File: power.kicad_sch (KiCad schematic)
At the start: 75 parts, among them SW1 SW_Push, U3 BD71847MWV, U4 NCP718BSN250T1G, Y1 Crystal

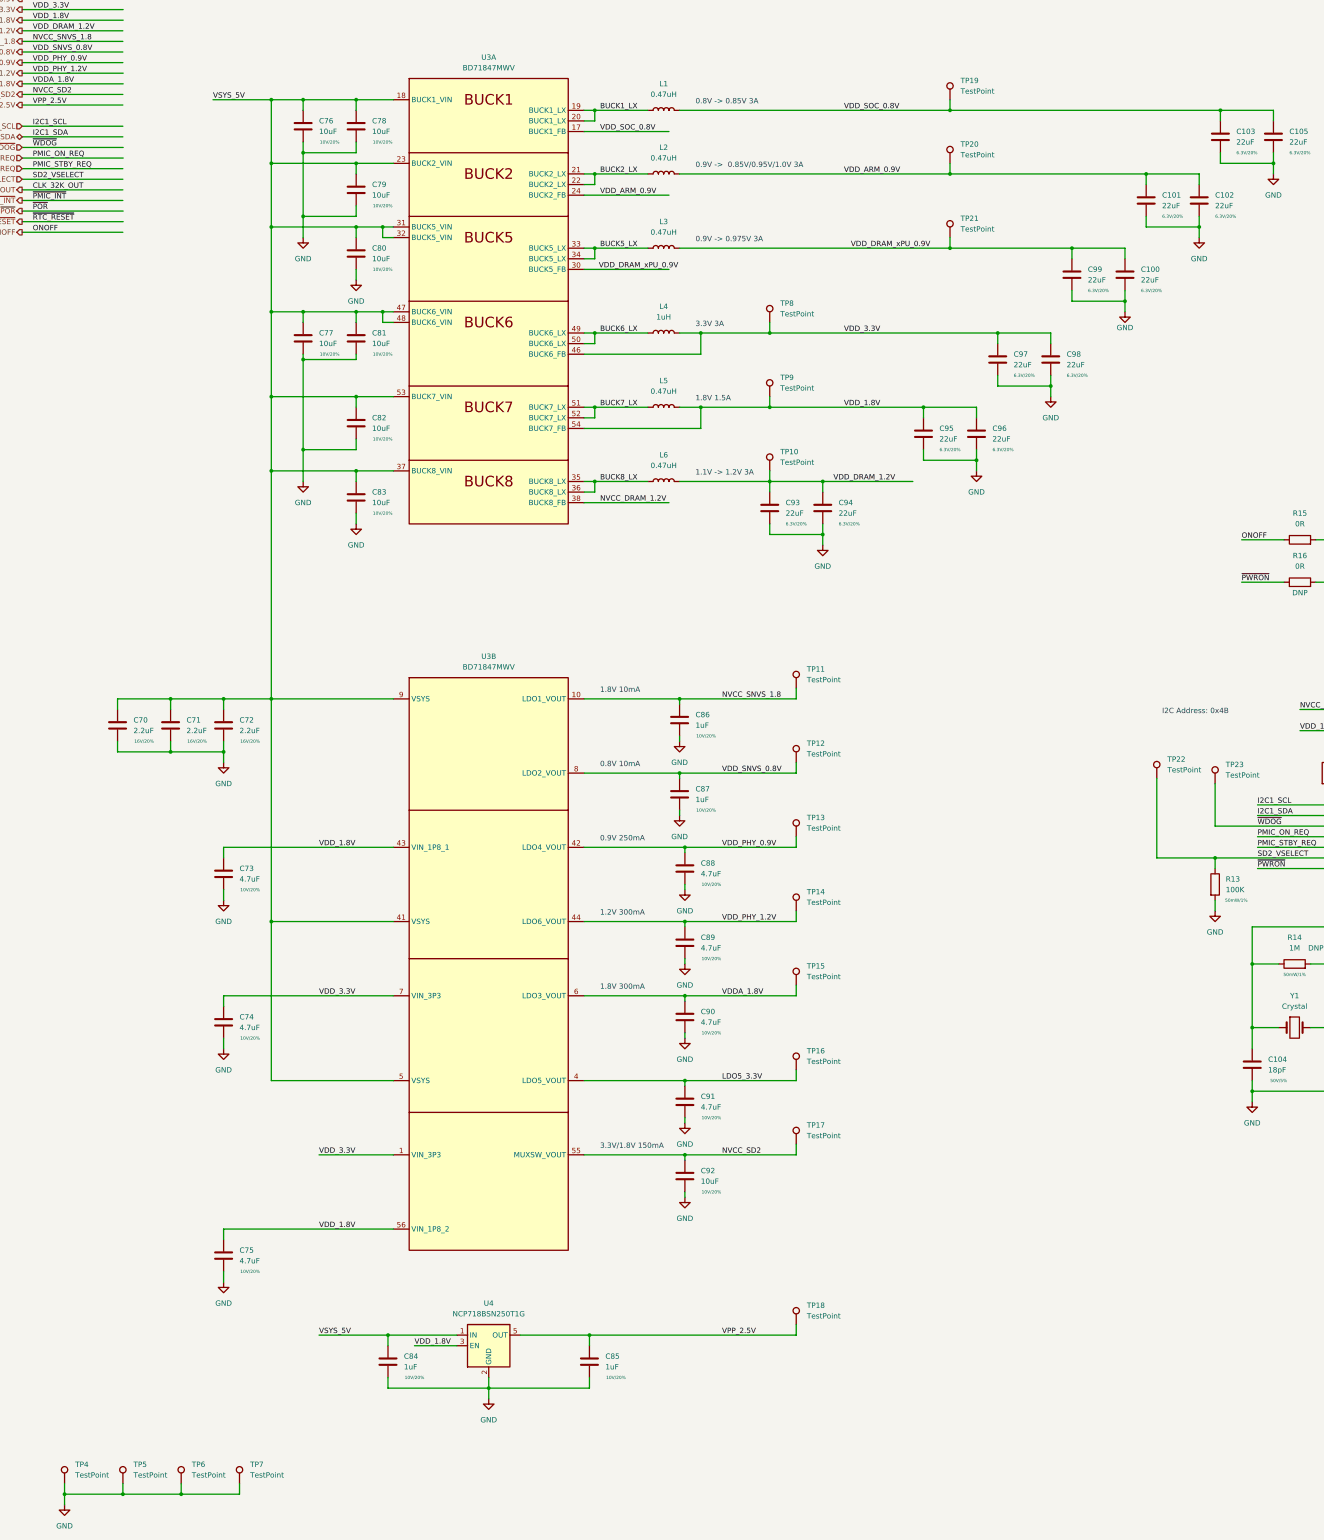
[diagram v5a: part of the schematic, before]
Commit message: v2 of ddr flytimes tool, lots of routing work, sch fixes
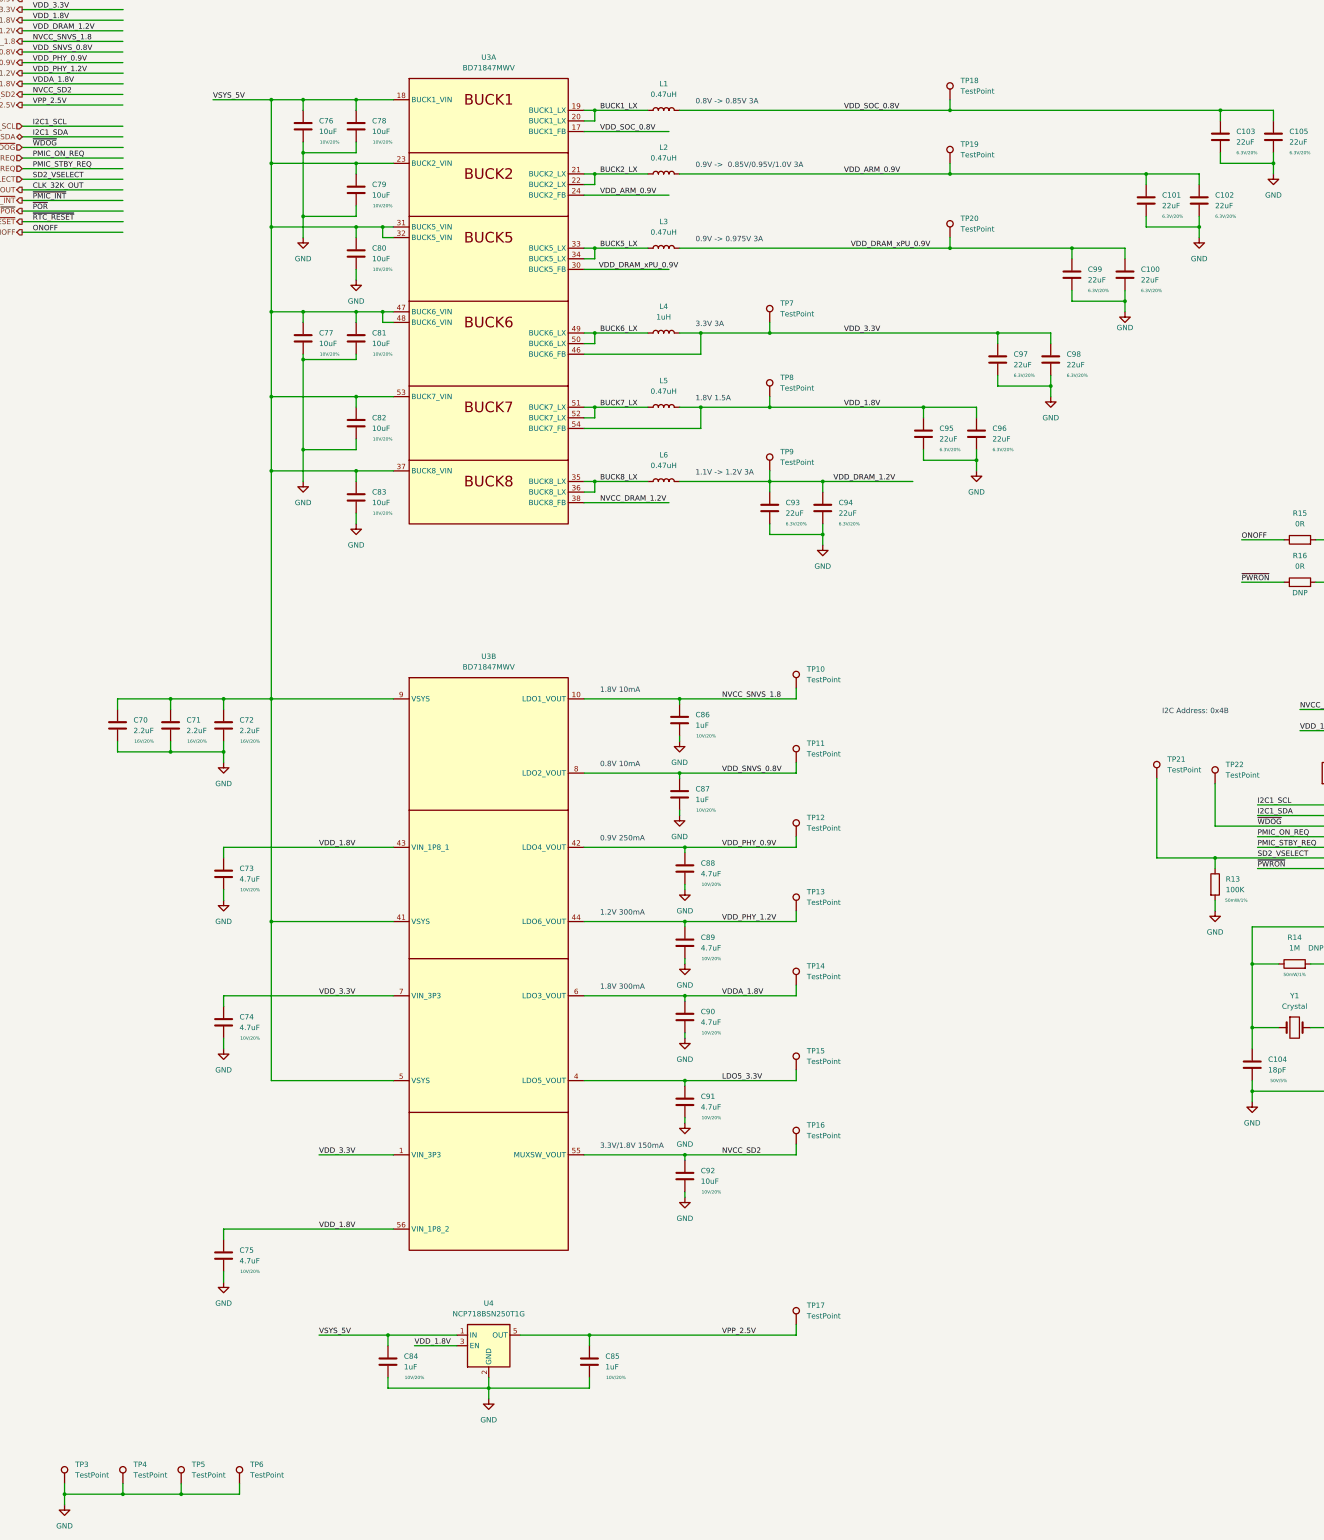
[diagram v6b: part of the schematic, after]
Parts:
- renumbered TP11 to TP10, TP12 to TP11, TP13 to TP12, TP14 to TP13, TP15 to TP14, TP16 to TP15, TP17 to TP16, TP18 to TP17, TP19 to TP18, TP20 to TP19, TP21 to TP20, TP22 to TP21, TP23 to TP22, TP4 to TP3, TP5 to TP4, TP6 to TP5, TP7 to TP6, TP8 to TP7, TP9 to TP8, TP10 to TP9
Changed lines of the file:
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@@
   (symbol (lib_id "Connector:TestPoint") (at 257.81 49.53 0) (unit 1)
     (in_bom yes) (on_board yes) (fields_autoplaced)
-    (property "Reference" "TP19" (id 0) (at 260.35 44.9579 0)
+    (property "Reference" "TP18" (id 0) (at 260.35 44.9579 0)
       (effects (font (size 1.27 1.27)) (justify left))
     )
@@
   (symbol (lib_id "Connector:TestPoint") (at 73.66 381 0) (unit 1)
     (in_bom yes) (on_board yes) (fields_autoplaced)
-    (property "Reference" "TP6" (id 0) (at 76.2 376.4279 0)
+    (property "Reference" "TP5" (id 0) (at 76.2 376.4279 0)
       (effects (font (size 1.27 1.27)) (justify left))
     )
@@
   (symbol (lib_id "Connector:TestPoint") (at 220.98 281.94 0) (unit 1)
     (in_bom yes) (on_board yes) (fields_autoplaced)
-    (property "Reference" "TP16" (id 0) (at 223.52 277.3679 0)
+    (property "Reference" "TP15" (id 0) (at 223.52 277.3679 0)
       (effects (font (size 1.27 1.27)) (justify left))
     )
@@
   (symbol (lib_id "Connector:TestPoint") (at 220.98 226.06 0) (unit 1)
     (in_bom yes) (on_board yes) (fields_autoplaced)
-    (property "Reference" "TP13" (id 0) (at 223.52 221.4879 0)
+    (property "Reference" "TP12" (id 0) (at 223.52 221.4879 0)
       (effects (font (size 1.27 1.27)) (justify left))
     )
@@
   (symbol (lib_id "Connector:TestPoint") (at 59.69 381 0) (unit 1)
     (in_bom yes) (on_board yes) (fields_autoplaced)
-    (property "Reference" "TP5" (id 0) (at 62.23 376.4279 0)
+    (property "Reference" "TP4" (id 0) (at 62.23 376.4279 0)
       (effects (font (size 1.27 1.27)) (justify left))
     )
@@
   (symbol (lib_id "Connector:TestPoint") (at 45.72 381 0) (unit 1)
     (in_bom yes) (on_board yes) (fields_autoplaced)
-    (property "Reference" "TP4" (id 0) (at 48.26 376.4279 0)
+    (property "Reference" "TP3" (id 0) (at 48.26 376.4279 0)
       (effects (font (size 1.27 1.27)) (justify left))
     )
@@
   (symbol (lib_id "Connector:TestPoint") (at 220.98 299.72 0) (unit 1)
     (in_bom yes) (on_board yes) (fields_autoplaced)
-    (property "Reference" "TP17" (id 0) (at 223.52 295.1479 0)
+    (property "Reference" "TP16" (id 0) (at 223.52 295.1479 0)
       (effects (font (size 1.27 1.27)) (justify left))
     )
@@
   (symbol (lib_id "Connector:TestPoint") (at 214.63 102.87 0) (unit 1)
     (in_bom yes) (on_board yes) (fields_autoplaced)
-    (property "Reference" "TP8" (id 0) (at 217.17 98.2979 0)
+    (property "Reference" "TP7" (id 0) (at 217.17 98.2979 0)
       (effects (font (size 1.27 1.27)) (justify left))
     )
@@
   (symbol (lib_id "Connector:TestPoint") (at 220.98 342.9 0) (unit 1)
     (in_bom yes) (on_board yes) (fields_autoplaced)
-    (property "Reference" "TP18" (id 0) (at 223.52 338.3279 0)
+    (property "Reference" "TP17" (id 0) (at 223.52 338.3279 0)
       (effects (font (size 1.27 1.27)) (justify left))
     )
@@
   (symbol (lib_id "Connector:TestPoint") (at 257.81 82.55 0) (unit 1)
     (in_bom yes) (on_board yes) (fields_autoplaced)
-    (property "Reference" "TP21" (id 0) (at 260.35 77.9779 0)
+    (property "Reference" "TP20" (id 0) (at 260.35 77.9779 0)
       (effects (font (size 1.27 1.27)) (justify left))
     )
@@
   (symbol (lib_id "Connector:TestPoint") (at 220.98 261.62 0) (unit 1)
     (in_bom yes) (on_board yes) (fields_autoplaced)
-    (property "Reference" "TP15" (id 0) (at 223.52 257.0479 0)
+    (property "Reference" "TP14" (id 0) (at 223.52 257.0479 0)
       (effects (font (size 1.27 1.27)) (justify left))
     )
@@
   (symbol (lib_id "Connector:TestPoint") (at 220.98 190.5 0) (unit 1)
     (in_bom yes) (on_board yes) (fields_autoplaced)
-    (property "Reference" "TP11" (id 0) (at 223.52 185.9279 0)
+    (property "Reference" "TP10" (id 0) (at 223.52 185.9279 0)
       (effects (font (size 1.27 1.27)) (justify left))
     )
@@
   (symbol (lib_id "Connector:TestPoint") (at 214.63 120.65 0) (unit 1)
     (in_bom yes) (on_board yes) (fields_autoplaced)
-    (property "Reference" "TP9" (id 0) (at 217.17 116.0779 0)
+    (property "Reference" "TP8" (id 0) (at 217.17 116.0779 0)
       (effects (font (size 1.27 1.27)) (justify left))
     )
@@
   (symbol (lib_id "Connector:TestPoint") (at 257.81 64.77 0) (unit 1)
     (in_bom yes) (on_board yes) (fields_autoplaced)
-    (property "Reference" "TP20" (id 0) (at 260.35 60.1979 0)
+    (property "Reference" "TP19" (id 0) (at 260.35 60.1979 0)
       (effects (font (size 1.27 1.27)) (justify left))
     )
@@
   (symbol (lib_id "Connector:TestPoint") (at 220.98 208.28 0) (unit 1)
     (in_bom yes) (on_board yes) (fields_autoplaced)
-    (property "Reference" "TP12" (id 0) (at 223.52 203.7079 0)
+    (property "Reference" "TP11" (id 0) (at 223.52 203.7079 0)
       (effects (font (size 1.27 1.27)) (justify left))
     )
@@
   (symbol (lib_id "Connector:TestPoint") (at 87.63 381 0) (unit 1)
     (in_bom yes) (on_board yes) (fields_autoplaced)
-    (property "Reference" "TP7" (id 0) (at 90.17 376.4279 0)
+    (property "Reference" "TP6" (id 0) (at 90.17 376.4279 0)
       (effects (font (size 1.27 1.27)) (justify left))
     )
@@
   (symbol (lib_id "Connector:TestPoint") (at 220.98 243.84 0) (unit 1)
     (in_bom yes) (on_board yes) (fields_autoplaced)
-    (property "Reference" "TP14" (id 0) (at 223.52 239.2679 0)
+    (property "Reference" "TP13" (id 0) (at 223.52 239.2679 0)
       (effects (font (size 1.27 1.27)) (justify left))
     )
@@
   (symbol (lib_id "Connector:TestPoint") (at 307.34 212.09 0) (unit 1)
     (in_bom yes) (on_board yes) (fields_autoplaced)
-    (property "Reference" "TP22" (id 0) (at 309.88 207.5179 0)
+    (property "Reference" "TP21" (id 0) (at 309.88 207.5179 0)
       (effects (font (size 1.27 1.27)) (justify left))
     )
@@
   (symbol (lib_id "Connector:TestPoint") (at 321.31 213.36 0) (unit 1)
     (in_bom yes) (on_board yes) (fields_autoplaced)
-    (property "Reference" "TP23" (id 0) (at 323.85 208.7879 0)
+    (property "Reference" "TP22" (id 0) (at 323.85 208.7879 0)
       (effects (font (size 1.27 1.27)) (justify left))
     )
@@
   (symbol (lib_id "Connector:TestPoint") (at 214.63 138.43 0) (unit 1)
     (in_bom yes) (on_board yes) (fields_autoplaced)
-    (property "Reference" "TP10" (id 0) (at 217.17 133.8579 0)
-      (effects (font (size 1.27 1.27)) (justify left))
-    )
+    (property "Reference" "TP9" (id 0) (at 217.17 133.8579 0)
+      (effects (font (size 1.27 1.27)) (justify left))
+    )

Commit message: inital routing of ddr data bus, sch work
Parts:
- removed C84, C85: 1uF, Capacitor_SMD:C_0402_1005Metric, symbol Device:C
- removed TP17: TestPoint, TestPoint:TestPoint_Pad_D1.0mm, symbol Connector:TestPoint
- removed U4: NCP718BSN250T1G, Package_TO_SOT_SMD:SOT-23-5, symbol Regulator_Linear:NCP718xSN250
- renumbered C70 to C58, C71 to C59, C72 to C60, C73 to C61, C74 to C62, C75 to C63, C76 to C64, C77 to C65, C78 to C66, C79 to C67, C80 to C68, C81 to C69, C82 to C70, C83 to C71, C86 to C72, C87 to C73, C88 to C74, C89 to C75, C90 to C76, C91 to C77, C92 to C78, C93 to C79, C94 to C80, C95 to C81, C96 to C82, C97 to C83, C98 to C84, C99 to C85, C100 to C86, C101 to C87, C102 to C88, C103 to C89, C104 to C90, C105 to C91, C106 to C92, C107 to C93, C108 to C94, R13 to R11, R14 to R12, R15 to R13, R16 to R14, R17 to R15, R18 to R16, TP11 to TP10, TP12 to TP11, TP13 to TP12, TP14 to TP13, TP15 to TP14, TP16 to TP15, TP18 to TP16, TP19 to TP17, TP20 to TP18, TP21 to TP19, TP3 to TP2, TP22 to TP20, TP4 to TP3, TP5 to TP4, TP6 to TP5, TP7 to TP6, TP8 to TP7, TP9 to TP8, TP10 to TP9
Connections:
- net VDD_DRAM_1.2V renamed VDD_DRAM_1.1V

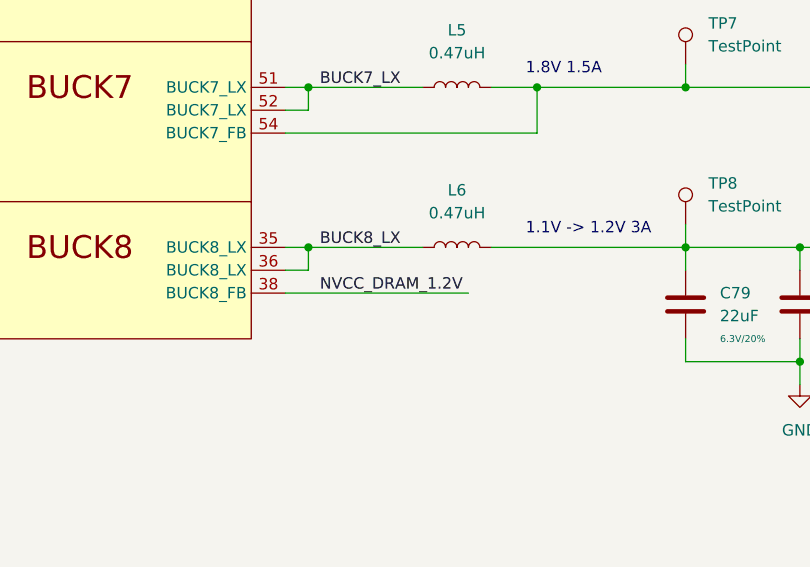
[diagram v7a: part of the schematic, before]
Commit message: add SN65DSI86 DSI2DP ic, SCH, PCB work, flytime work
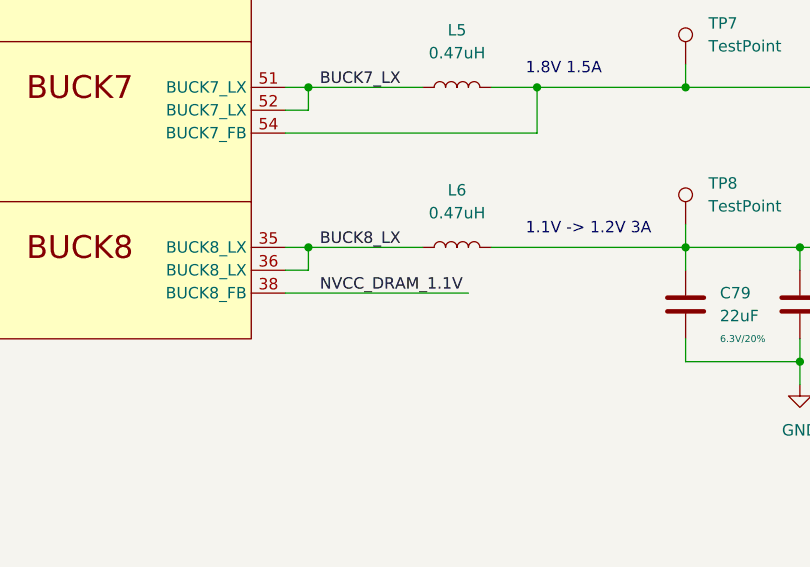
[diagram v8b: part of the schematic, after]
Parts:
- SW1: footprint Button_Switch_THT:SW_Tactile_SPST_Angled_PTS645Vx58-2LFS -> Button_Switch_SMD:SW_SPST_EVQP7A
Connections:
- net NVCC_DRAM_1.2V renamed NVCC_DRAM_1.1V
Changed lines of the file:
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@@
     (effects (font (size 1.27 1.27)) (justify left bottom))
   )
-  (label "NVCC_DRAM_1.2V" (at 173.99 146.05 0)
+  (label "NVCC_DRAM_1.1V" (at 173.99 146.05 0)
     (effects (font (size 1.27 1.27)) (justify left bottom))
   )
@@
     (property "Reference" "SW1" (id 0) (at 360.68 147.32 0))
     (property "Value" "SW_Push" (id 1) (at 360.68 149.86 0))
-    (property "Footprint" "Button_Switch_THT:SW_Tactile_SPST_Angled_PTS645Vx58-2LFS" (id 2) (at 360.68 149.86 0)
-      (effects (font (size 1.27 1.27)) hide)
-    )
+    (property "Footprint" "Button_Switch_SMD:SW_SPST_EVQP7A" (id 2) (at 360.68 149.86 0)
+      (effects (font (size 1.27 1.27)) hide)
+    )
